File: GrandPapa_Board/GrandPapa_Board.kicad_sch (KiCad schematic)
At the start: 14 parts, among them J11 Dupont 01x04_Male, J2 HARWIN CONN, J3 Dupont 01x06_Female, J4 HARWIN CONN, J5 Dupont 01x06_Female, J7 HARWIN CONN

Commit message: fix comments
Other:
- note removed: "Max Iout 300 mA"
- note removed: "Max power draw on MCU is 170 mA @ 3.3V, +85°C see pg 684 of datasheet Max power draw on ATA6561 CAN transciever is 70 mA"
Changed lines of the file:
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@@
     (stroke (width 0) (type default) (color 0 0 0 0))
-  )
-  (text "Max power draw on \nMCU is 170 mA\n@ 3.3V, +85°C\nsee pg 684 of datasheet\nMax power draw on ATA6561 \nCAN transciever is 70 mA"
-    (at 248.92 111.76 0)
-    (effects (font (size 1.27 1.27)) (justify left bottom))
   )
   (text "Logger Board" (at 248.285 31.75 0)
@@
     (effects (font (size 1.27 1.27) bold) (justify left bottom))
   )
-  (text "Max Iout 300 mA\n" (at 248.92 114.3 0)
-    (effects (font (size 1.27 1.27) (thickness 0.254) bold) (justify left bottom))
-  )
   (label "CANH_PAYLOAD" (at 241.935 35.56 180)

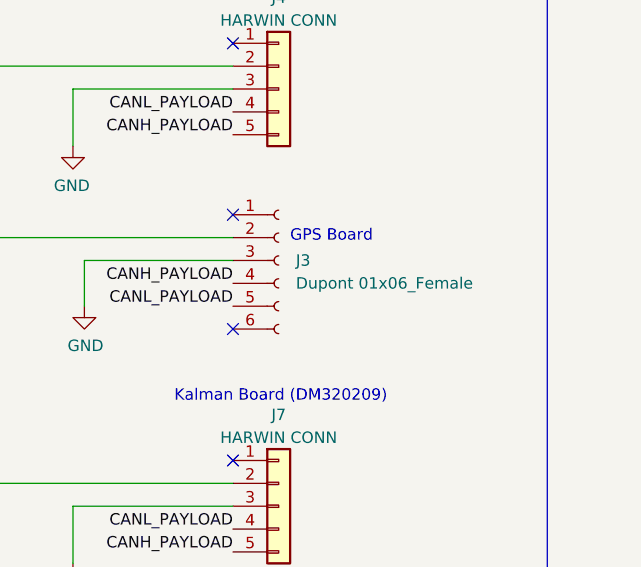
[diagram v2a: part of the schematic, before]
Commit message: Add footprints, inductors TBD
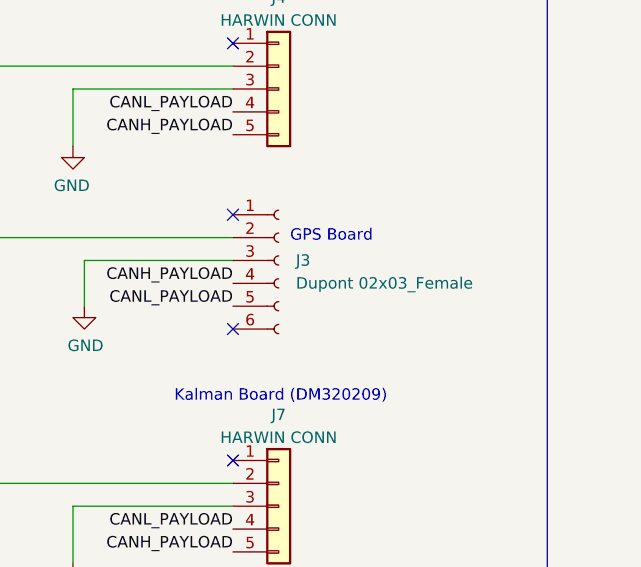
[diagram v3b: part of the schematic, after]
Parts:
- H1, H2, H3, H4, H5, H6, H7, H8: footprint (none) -> MountingHole:MountingHole_3.5mm_Pad_Via
- J11: footprint (none) -> Connector_PinHeader_2.54mm:PinHeader_1x04_P2.54mm_Vertical
- J3: value Dupont 01x06_Female -> Dupont 02x03_Female; footprint (none) -> PapaOld:PinHeader_2x03_P2.00mm_Vertical_MINISENSOR_Harwin_Spacing
- J5: footprint (none) -> PapaOld:PinHeader_2x03_P2.00mm_Vertical_MINISENSOR_Harwin_Spacing

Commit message: add footprints, group layouts
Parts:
- J2: value HARWIN CONN -> HARWIN_ROCKET; footprint Payload2020_custom:connector_Harwin_M80-5000642 -> PapaOld:connector_Harwin_M80-5000642
- J4: value HARWIN CONN -> HARWIN_MINISENSOR; footprint Payload2020_custom:connector_Harwin_M80-5000642 -> PapaOld:connector_Harwin_M80-5000642
- J7: value HARWIN CONN -> HARWIN_KALMAN; footprint Payload2020_custom:connector_Harwin_M80-5000642 -> PapaOld:connector_Harwin_M80-5000642
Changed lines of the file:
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@@
     (in_bom yes) (on_board yes)
     (property "Reference" "J7" (id 0) (at 247.015 93.345 0))
-    (property "Value" "HARWIN CONN" (id 1) (at 247.015 95.885 0))
-    (property "Footprint" "Payload2020_custom:connector_Harwin_M80-5000642" (id 2) (at 247.015 103.505 0)
+    (property "Value" "HARWIN_KALMAN" (id 1) (at 247.015 95.885 0))
+    (property "Footprint" "PapaOld:connector_Harwin_M80-5000642" (id 2) (at 247.015 103.505 0)
       (effects (font (size 1.27 1.27)) hide)
     )
@@
     (in_bom yes) (on_board yes)
     (property "Reference" "J4" (id 0) (at 247.015 46.99 0))
-    (property "Value" "HARWIN CONN" (id 1) (at 247.015 49.53 0))
-    (property "Footprint" "Payload2020_custom:connector_Harwin_M80-5000642" (id 2) (at 247.015 57.15 0)
+    (property "Value" "HARWIN_MINISENSOR" (id 1) (at 247.015 49.53 0))
+    (property "Footprint" "PapaOld:connector_Harwin_M80-5000642" (id 2) (at 247.015 57.15 0)
       (effects (font (size 1.27 1.27)) hide)
     )
@@
     (in_bom yes) (on_board yes)
     (property "Reference" "J2" (id 0) (at 42.545 34.925 0))
-    (property "Value" "HARWIN CONN" (id 1) (at 42.545 37.465 0))
-    (property "Footprint" "Payload2020_custom:connector_Harwin_M80-5000642" (id 2) (at 42.545 46.355 0)
+    (property "Value" "HARWIN_ROCKET" (id 1) (at 42.545 37.465 0))
+    (property "Footprint" "PapaOld:connector_Harwin_M80-5000642" (id 2) (at 42.545 46.355 0)
       (effects (font (size 1.27 1.27)) hide)
     )
@@
       (reference "#PWR0101") (unit 1) (value "+5V") (footprint "")
     )
+    (path "/6da90ef0-c465-4ff3-9b37-6e85282e96ed/fe05a526-136d-4cf2-9827-793ff06e3cc8"
+      (reference "#PWR0102") (unit 1) (value "GND") (footprint "")
+    )
     (path "/6e3b0b39-ae79-433b-961a-4cecb7d81a21/650f6504-e891-4404-a660-ac0fb77c96a7"
       (reference "#PWR0108") (unit 1) (value "GND") (footprint "")
@@
       (reference "#PWR0110") (unit 1) (value "GND") (footprint "")
     )
-    (path "/6da90ef0-c465-4ff3-9b37-6e85282e96ed/fe05a526-136d-4cf2-9827-793ff06e3cc8"
-      (reference "#PWR?") (unit 1) (value "GND") (footprint "")
-    )
     (path "/6da90ef0-c465-4ff3-9b37-6e85282e96ed/53ba3d92-1a41-4a88-9613-15e75aad5f25"
       (reference "C1") (unit 1) (value "10uF") (footprint "Capacitor_SMD:C_0805_2012Metric_Pad1.18x1.45mm_HandSolder")
@@
     )
     (path "/9b3c8cdd-eebb-48dc-9103-b9751ef4664e"
-      (reference "J2") (unit 1) (value "HARWIN CONN") (footprint "Payload2020_custom:connector_Harwin_M80-5000642")
+      (reference "J2") (unit 1) (value "HARWIN_ROCKET") (footprint "PapaOld:connector_Harwin_M80-5000642")
     )
     (path "/bc115b77-66ba-4ad5-9769-e8d4d5e7e0d1"
@@
     )
     (path "/9148568f-147d-473b-b021-8ad960db1440"
-      (reference "J4") (unit 1) (value "HARWIN CONN") (footprint "Payload2020_custom:connector_Harwin_M80-5000642")
+      (reference "J4") (unit 1) (value "HARWIN_MINISENSOR") (footprint "PapaOld:connector_Harwin_M80-5000642")
     )
     (path "/a8426bc2-c0da-425a-9644-1cdd24d3376a"
@@
     )
     (path "/426d6114-d3b8-47a3-9389-3c2fec82ed9d"
-      (reference "J7") (unit 1) (value "HARWIN CONN") (footprint "Payload2020_custom:connector_Harwin_M80-5000642")
+      (reference "J7") (unit 1) (value "HARWIN_KALMAN") (footprint "PapaOld:connector_Harwin_M80-5000642")
     )
     (path "/2746e30c-cf47-4b9c-9f99-0aa497348790"
@@
     )
     (path "/6da90ef0-c465-4ff3-9b37-6e85282e96ed/dd7fe674-7ec5-4f4e-bae0-71ca9493043e"
-      (reference "R8") (unit 1) (value "10k") (footprint "Resistor_SMD:R_0805_2012Metric_Pad1.20x1.40mm_HandSolder")
+      (reference "R8") (unit 1) (value "10kR") (footprint "Resistor_SMD:R_0805_2012Metric_Pad1.20x1.40mm_HandSolder")
     )
     (path "/6da90ef0-c465-4ff3-9b37-6e85282e96ed/cdf659c0-d404-4008-8040-a75e802f2f5e"
@@
     )
     (path "/6da90ef0-c465-4ff3-9b37-6e85282e96ed/a4dbde3b-7159-4f1a-8883-300fc4fc0b48"
-      (reference "R27") (unit 1) (value "15k") (footprint "Resistor_SMD:R_0805_2012Metric_Pad1.20x1.40mm_HandSolder")
+      (reference "R27") (unit 1) (value "15kR") (footprint "Resistor_SMD:R_0805_2012Metric_Pad1.20x1.40mm_HandSolder")
     )
     (path "/9000e807-73a6-4445-a3d9-68a08e981f82/d86a5dda-66ea-4311-a7d2-5e2cf0558120"

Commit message: change stackup, mounting holes, connector footprints, power reg layout, fuse values
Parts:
- J3, J5: footprint PapaOld:PinHeader_2x03_P2.00mm_Vertical_MINISENSOR_Harwin_Spacing -> PapaOld:connector_Harwin_M80-5000642
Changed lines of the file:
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@@
       (effects (font (size 1.27 1.27)) (justify left))
     )
-    (property "Footprint" "PapaOld:PinHeader_2x03_P2.00mm_Vertical_MINISENSOR_Harwin_Spacing" (id 2) (at 247.015 33.02 0)
+    (property "Footprint" "PapaOld:connector_Harwin_M80-5000642" (id 2) (at 247.015 33.02 0)
       (effects (font (size 1.27 1.27)) hide)
     )
@@
       (effects (font (size 1.27 1.27)) (justify left))
     )
-    (property "Footprint" "PapaOld:PinHeader_2x03_P2.00mm_Vertical_MINISENSOR_Harwin_Spacing" (id 2) (at 247.015 76.2 0)
+    (property "Footprint" "PapaOld:connector_Harwin_M80-5000642" (id 2) (at 247.015 76.2 0)
       (effects (font (size 1.27 1.27)) hide)
     )
@@
     )
     (path "/6da90ef0-c465-4ff3-9b37-6e85282e96ed/c52fdc02-e0a8-4618-a9e4-68265e3d6d1e"
-      (reference "F1") (unit 1) (value "1.2A") (footprint "Fuse:Fuse_0805_2012Metric_Pad1.15x1.40mm_HandSolder")
+      (reference "F1") (unit 1) (value "1.5A") (footprint "Fuse:Fuse_0805_2012Metric_Pad1.15x1.40mm_HandSolder")
     )
     (path "/6da90ef0-c465-4ff3-9b37-6e85282e96ed/809480a9-88b8-4969-9c58-8122901dfc7f"
@@
     )
     (path "/9000e807-73a6-4445-a3d9-68a08e981f82/7d6337a6-d33d-4597-b113-21a9991d2059"
-      (reference "F3") (unit 1) (value "1.2A") (footprint "Fuse:Fuse_0805_2012Metric_Pad1.15x1.40mm_HandSolder")
+      (reference "F3") (unit 1) (value "1.5A") (footprint "Fuse:Fuse_0805_2012Metric_Pad1.15x1.40mm_HandSolder")
     )
     (path "/0595b1c1-a330-42a2-a1cc-5d884417ccf0"
@@
     )
     (path "/bc115b77-66ba-4ad5-9769-e8d4d5e7e0d1"
-      (reference "J3") (unit 1) (value "Dupont 02x03_Female") (footprint "PapaOld:PinHeader_2x03_P2.00mm_Vertical_MINISENSOR_Harwin_Spacing")
+      (reference "J3") (unit 1) (value "Dupont 02x03_Female") (footprint "PapaOld:connector_Harwin_M80-5000642")
     )
     (path "/9148568f-147d-473b-b021-8ad960db1440"
@@
     )
     (path "/a8426bc2-c0da-425a-9644-1cdd24d3376a"
-      (reference "J5") (unit 1) (value "Dupont 01x06_Female") (footprint "PapaOld:PinHeader_2x03_P2.00mm_Vertical_MINISENSOR_Harwin_Spacing")
+      (reference "J5") (unit 1) (value "Dupont 01x06_Female") (footprint "PapaOld:connector_Harwin_M80-5000642")
     )
     (path "/6e3b0b39-ae79-433b-961a-4cecb7d81a21/9d46a4f7-4238-467d-b81e-da5f8cd8a079"

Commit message: update layout + routing
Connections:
- net CANH_PAYLOAD: now also J4.4 (Pin_4), J7.4 (Pin_4); no longer J4.5 (Pin_5), J7.5 (Pin_5)
- net CANL_PAYLOAD: now also J4.5 (Pin_5), J7.5 (Pin_5); no longer J4.4 (Pin_4), J7.4 (Pin_4)
- net MCU and CAN Controllers/CANH_ROCKET: now also J2.4 (Pin_4); no longer J2.5 (Pin_5)
- net MCU and CAN Controllers/CANL_ROCKET: now also J2.5 (Pin_5); no longer J2.4 (Pin_4)
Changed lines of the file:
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@@
     (effects (font (size 1.27 1.27) bold) (justify left bottom))
+  )
+  (label "CANL_PAYLOAD" (at 66.04 109.22 180)
+    (effects (font (size 1.27 1.27)) (justify right bottom))
   )
   (label "CANH_PAYLOAD" (at 241.935 35.56 180)
     (effects (font (size 1.27 1.27)) (justify right bottom))
   )
-  (label "CANH_PAYLOAD" (at 241.935 108.585 180)
+  (label "CANL_PAYLOAD" (at 241.935 108.585 180)
+    (effects (font (size 1.27 1.27)) (justify right bottom))
+  )
+  (label "CANL_PAYLOAD" (at 241.935 81.28 180)
+    (effects (font (size 1.27 1.27)) (justify right bottom))
+  )
+  (label "CANH_PAYLOAD" (at 241.935 78.74 180)
+    (effects (font (size 1.27 1.27)) (justify right bottom))
+  )
+  (label "CANH_PAYLOAD" (at 241.935 106.045 180)
     (effects (font (size 1.27 1.27)) (justify right bottom))
   )
@@
     (effects (font (size 1.27 1.27)) (justify right bottom))
   )
-  (label "CANL_PAYLOAD" (at 241.935 81.28 180)
-    (effects (font (size 1.27 1.27)) (justify right bottom))
-  )
-  (label "CANH_PAYLOAD" (at 241.935 78.74 180)
-    (effects (font (size 1.27 1.27)) (justify right bottom))
-  )
-  (label "CANL_PAYLOAD" (at 241.935 106.045 180)
-    (effects (font (size 1.27 1.27)) (justify right bottom))
-  )
   (label "CANL_PAYLOAD" (at 241.935 38.1 180)
     (effects (font (size 1.27 1.27)) (justify right bottom))
   )
-  (label "CANL_PAYLOAD" (at 66.04 109.22 180)
+  (label "CANH_PAYLOAD" (at 241.935 59.69 180)
     (effects (font (size 1.27 1.27)) (justify right bottom))
   )
-  (label "CANL_PAYLOAD" (at 241.935 59.69 180)
-    (effects (font (size 1.27 1.27)) (justify right bottom))
-  )
-  (label "CANH_PAYLOAD" (at 241.935 62.23 180)
+  (label "CANL_PAYLOAD" (at 241.935 62.23 180)
     (effects (font (size 1.27 1.27)) (justify right bottom))
   )
@@
       (effects (font (size 1.27 1.27)) (justify left))
     )
-    (pin "CANH_ROCKET" input (at 66.04 95.25 180)
-      (effects (font (size 1.27 1.27)) (justify left))
-    )
-    (pin "CANL_ROCKET" input (at 66.04 92.71 180)
+    (pin "CANL_ROCKET" input (at 66.04 95.25 180)
+      (effects (font (size 1.27 1.27)) (justify left))
+    )
+    (pin "CANH_ROCKET" input (at 66.04 92.71 180)
       (effects (font (size 1.27 1.27)) (justify left))
     )
@@
       (reference "TP2") (unit 1) (value "TestPoint") (footprint "Connector_PinHeader_2.54mm:PinHeader_1x01_P2.54mm_Vertical")
     )
-    (path "/6da90ef0-c465-4ff3-9b37-6e85282e96ed/7d4109e7-1069-45c5-bd1b-4e164720ec3a"
+    (path "/6da90ef0-c465-4ff3-9b37-6e85282e96ed/7ae2fca9-1790-4ac9-96a1-3380e124f0d7"
       (reference "TP3") (unit 1) (value "TestPoint") (footprint "Connector_PinHeader_2.54mm:PinHeader_1x01_P2.54mm_Vertical")
     )
